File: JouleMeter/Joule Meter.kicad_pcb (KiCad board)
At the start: 4 copper layers, 120 x 134.6 mm, 82 parts, among them J1 XT60-M, J2 XT60-M, J3 22035035, J4 22035035, U1 LMR36510, U3 INA240A1PW, U4 ADS1118IDGS-Q1, U5 MCP6286T-E/OT1

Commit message: Patrick Feedback
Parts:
- removed TP14: VF-V-, TestPoint:TestPoint_Pad_1.0x1.0mm
- moved R12 22.5 mm to (131.3, 64.5), turned to -90 degrees
- moved TP3 19.8 mm to (88.0, 37.0)
- moved C4 15.5 mm to (108.5, 39.0)
- moved TP21 13.3 mm to (128.6, 69.5)
- moved R8 10.5 mm to (116.5, 83.5), turned to 0 degrees
- moved R9 10.4 mm to (131.6, 69.5)
- moved R7 8.94 mm to (122.4, 83.8), turned to 0 degrees
- moved REF** 7.71 mm to (191.7, 163.2)
- moved Nucleo_F44RE2 7.71 mm to (151.6, 124.7)
- moved R13 7.71 mm to (187.9, 115.7)
- moved C20 6.96 mm to (189.9, 131.7)
- moved C22 6.96 mm to (187.9, 131.7)
- moved TP22 5.85 mm to (128.4, 74.0)
- moved TP23 5.85 mm to (128.4, 72.0)
- moved TP4 5.35 mm to (90.0, 71.0)
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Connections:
- U1 pad 16: (no net) -> GND
- U1 pad 9: unconnected-(U1-PAD-Pad9) -> GND
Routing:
- net /Voltage Follower: track 0.00 -> 17.7 mm
- net +3V3D: track 0.00 -> 15.5 mm, vias 0 -> 3
- net +3V3A: track 0.00 -> 13.5 mm, vias 0 -> 4
- net /Current_Sense: track 0.00 -> 13.1 mm
- net GND: track 0.00 -> 12.7 mm, vias 0 -> 12
- net /CS: track 0.00 -> 8.65 mm
- net Net-(U4-AIN1): track 0.00 -> 6.91 mm
- net Net-(J1-POS): track 0.00 -> 6.88 mm
- net Net-(U4-AIN0): track 0.00 -> 6.70 mm
- net Net-(U5-+): track 0.00 -> 6.67 mm
- net Net-(U1-VCC): track 0.00 -> 6.61 mm
- net /FB: track 0.00 -> 6.37 mm
- net Net-(U1-BOOT): track 0.00 -> 6.16 mm
- net /MISO: track 0.00 -> 5.53 mm
- net Net-(J2-POS): track 0.00 -> 5.01 mm
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- added copper zone on F.Cu, net +3V3A
- added copper zone on In1.Cu, net +3V3A
- added copper zone on F.Cu, net +3V3D
- added copper zone on In1.Cu, net +3V3D
- added copper zone on F.Cu, net +5V
- added copper zone on In1.Cu, net +5V
- added copper zone on F.Cu, net +7V
- added copper zone on F.Cu, net Net-(U1-SW)
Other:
- board size 120 x 134.6 mm -> 120 x 143.7 mm

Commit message: Complete Draft Layout
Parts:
- added REF**: SEM_logo, SMV_Logo:SEM_logo, F.Cu at (97.2, 135.5)
- added TP14: VF-V-, TestPoint:TestPoint_Pad_1.0x1.0mm, F.Cu at (122.2, 56.8)
- FERITE_BEAD1: value FB2 -> FB1
- moved TP1 47.7 mm to (111.0, 78.5)
- moved TP3 19.0 mm to (106.8, 39.8)
- moved C4 14.9 mm to (93.8, 40.8)
- moved C2 14.7 mm to (117.2, 40.8)
- moved TP2 14.6 mm to (130.8, 39.0)
- moved REF** 9.21 mm to (78.2, 165.2)
- moved R8 7.50 mm to (122.4, 78.9)
- moved R7 6.79 mm to (122.5, 77.0), turned to 180 degrees
- moved C20 4.18 mm to (191.2, 127.7)
- moved C22 4.18 mm to (189.2, 127.7)
- moved R13 4.18 mm to (189.2, 111.7)
- moved Nucleo_F44RE2 4.06 mm to (152.8, 120.8)
- moved TP16 2.87 mm to (101.2, 80.5)
- moved C21 2.48 mm to (99.1, 84.3)
- moved C23 2.48 mm to (87.1, 79.3)
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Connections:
- net /CAN_H renamed /CAN_P
- net /CAN_L renamed /CAN_N
- C21 pad 1: +3V3D -> +3V3
- MCP2562 pad 5: +3V3D -> +3V3
- R13 pad 1: /Nucleo_F446RE/NUCLEO_1 -> Net-(Nucleo_F44RE2-VBAT)
- U1 pad 10: (no net) -> GND
- U1 pad 11: (no net) -> GND
- U1 pad 12: (no net) -> GND
- U1 pad 13: (no net) -> GND
- U1 pad 14: (no net) -> GND
- U1 pad 15: (no net) -> GND
- U1 pad 17: (no net) -> GND
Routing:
- net /CAN_RXD: track 0.00 -> 76.8 mm, vias 0 -> 1
- net /CAN-TXD: track 0.00 -> 75.4 mm, vias 0 -> 1
- net Net-(Nucleo_F44RE2-PA5): track 1.25 -> 62.2 mm
- net Net-(Nucleo_F44RE2-PA4): track 1.35 -> 62.3 mm
- net Net-(Nucleo_F44RE2-PA6): track 1.20 -> 62.0 mm
- net Net-(Nucleo_F44RE2-PA7): track 1.25 -> 62.0 mm
- net /CAN_N: track 0.00 -> 53.4 mm
- net /CAN_P: track 0.00 -> 48.8 mm
- net Net-(Nucleo_F44RE2-VBAT): track 0.00 -> 23.0 mm
- net /Nucleo_F446RE/NUCLEO_1: track 0.00 -> 14.4 mm
- net Net-(U4-AIN2): track 0.00 -> 7.53 mm
- net GND: track 12.7 -> 7.10 mm, vias 12 -> 344
- net +5V: track 1.71 -> 5.44 mm, vias 8 -> 9
- net Net-(J1-POS): track 6.88 -> 9.75 mm
- net +3V3: track 0.00 -> 2.25 mm
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- added copper zone on F.Cu, net GND
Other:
- board size 120 x 143.7 mm -> 120.5 x 143.7 mm
- board text added: "High Powered Joulemeter (w/Current Sense) 11/16/2025 University of California, Los Angeles By Sergio Gonzalez"
- board text removed: "By Sergio Gonzalez"

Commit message: PCB Complete Draft
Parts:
- removed TP19: CT-RXD, TestPoint:TestPoint_Pad_1.0x1.0mm
- removed TP20: CT-TXD, TestPoint:TestPoint_Pad_1.0x1.0mm
- added J5: M22-7130442, SMV_Joule:HARWIN_M22-7130442, F.Cu at (83.0, 79.1)
- moved R14 48.6 mm to (179.6, 79.5)
- moved TP18 48.3 mm to (176.4, 78.8), turned to 0 degrees
- moved R9 47.6 mm to (115.0, 114.9)
- moved TP21 47.5 mm to (112.2, 114.9), turned to 0 degrees
- moved TP22 45.8 mm to (112.1, 117.5), turned to 0 degrees
- moved R10 45.7 mm to (115.0, 117.5)
- moved TP23 43.2 mm to (112.2, 112.8), turned to 0 degrees
- moved R11 43.0 mm to (115.2, 112.7)
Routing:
- net /MISO: track 5.53 -> 78.1 mm, vias 0 -> 2
- net /SCLK: track 4.87 -> 76.5 mm, vias 0 -> 2
- net /MOSI: track 4.27 -> 74.8 mm, vias 0 -> 2
- net Net-(Nucleo_F44RE2-PA7): track 62.0 -> 7.93 mm, vias 1 -> 0
- net Net-(Nucleo_F44RE2-PA5): track 62.2 -> 8.62 mm, vias 1 -> 0
- net /CS: track 9.99 -> 60.7 mm, vias 0 -> 2
- net Net-(Nucleo_F44RE2-PA6): track 62.0 -> 13.2 mm, vias 1 -> 0
- net Net-(Nucleo_F44RE2-PA4): track 62.3 -> 14.1 mm, vias 1 -> 0
- net /CAN-TXD: track 75.4 -> 79.6 mm, vias 1 -> 0
- net /CAN_RXD: track 76.8 -> 79.6 mm, vias 1 -> 0
- net GND: vias 344 -> 349

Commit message: Revised Version Part 1
Implemented changes from Google Docs and Dylan
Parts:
- C19: value C19 -> 0.1uF
- R0: footprint SMV_Joule:WSBS8518_VIS-L -> SMV_Joule:RESC10052X145N
- U6: renamed from MCP2562; value U6 -> MCP2562
- moved R13 67.8 mm to (211.5, 47.7)
- moved J5 54.3 mm to (137.0, 85.0), turned to -90 degrees
- moved TP22 52.1 mm to (134.8, 70.7)
- moved R10 52.0 mm to (137.8, 70.7)
- moved TP23 50.0 mm to (134.7, 68.1)
- moved R11 49.9 mm to (137.8, 68.1)
- moved Nucleo_F44RE2 48.5 mm to (175.2, 77.8)
- moved REF** 48.2 mm to (213.0, 122.0)
- moved C20 48.1 mm to (213.6, 85.2)
- moved C22 48.1 mm to (211.6, 85.2)
- moved R14 47.8 mm to (195.2, 34.3)
- moved R9 47.2 mm to (137.8, 73.5)
- moved TP21 47.2 mm to (134.9, 73.5)
- moved TP18 46.9 mm to (191.5, 34.3)
- moved REF** 44.6 mm to (67.0, 122.0)
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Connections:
- C21 pad 1: +3V3 -> +3V3A
- U6 pad 5: +3V3 -> +3V3A
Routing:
- net /MISO: track 78.1 -> 17.7 mm, vias 2 -> 0
- net /CAN_RXD: track 79.6 -> 20.8 mm
- net /MOSI: track 74.8 -> 16.7 mm, vias 2 -> 0
- net /CAN-TXD: track 79.6 -> 24.4 mm
- net /SCLK: track 76.5 -> 24.7 mm
- net /CS: track 60.7 -> 95.8 mm, vias 2 -> 0
- net /Nucleo_F446RE/NUCLEO_1: track 14.4 -> 35.4 mm
- net Net-(Nucleo_F44RE2-VBAT): track 23.0 -> 4.55 mm
- net +7V: track 1.00 -> 11.8 mm
- net +3V3D: track 15.5 -> 4.91 mm
- net /Voltage Follower: track 17.7 -> 7.55 mm
- net /CAN_N: track 53.4 -> 46.1 mm
- net Net-(J1-POS): track 9.75 -> 2.58 mm, vias 0 -> 29
- net Net-(Nucleo_F44RE2-PA4): track 14.1 -> 20.0 mm
- net +5V: track 5.44 -> 11.3 mm
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- added copper zone on In2.Cu, net +3V3A
- added copper zone on In2.Cu, net +3V3D
- added copper zone on In2.Cu, net +5V
- added copper zone on In1.Cu, net GND
- added copper zone on B.Cu, net Net-(J1-POS)
- added copper zone on In2.Cu, net Net-(J1-POS)
- added copper zone on B.Cu, net Net-(J2-POS)
- added copper zone on In2.Cu, net Net-(J2-POS)
- removed copper zone on In1.Cu, net +3V3A
- removed copper zone on In1.Cu, net +3V3D
- removed copper zone on In1.Cu, net +5V
- removed copper zone on In2.Cu, net GND
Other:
- board size 120.5 x 143.7 mm -> 153.8 x 95 mm
- board text added: "High Power Joulemeter (w/Current Sense) 11/24/2025 University of California, Los Angeles By Sergio Gonzalez"
- board text removed: "High Powered Joulemeter (w/Current Sense) 11/16/2025 University of California, Los Angeles By Sergio Gonzalez"

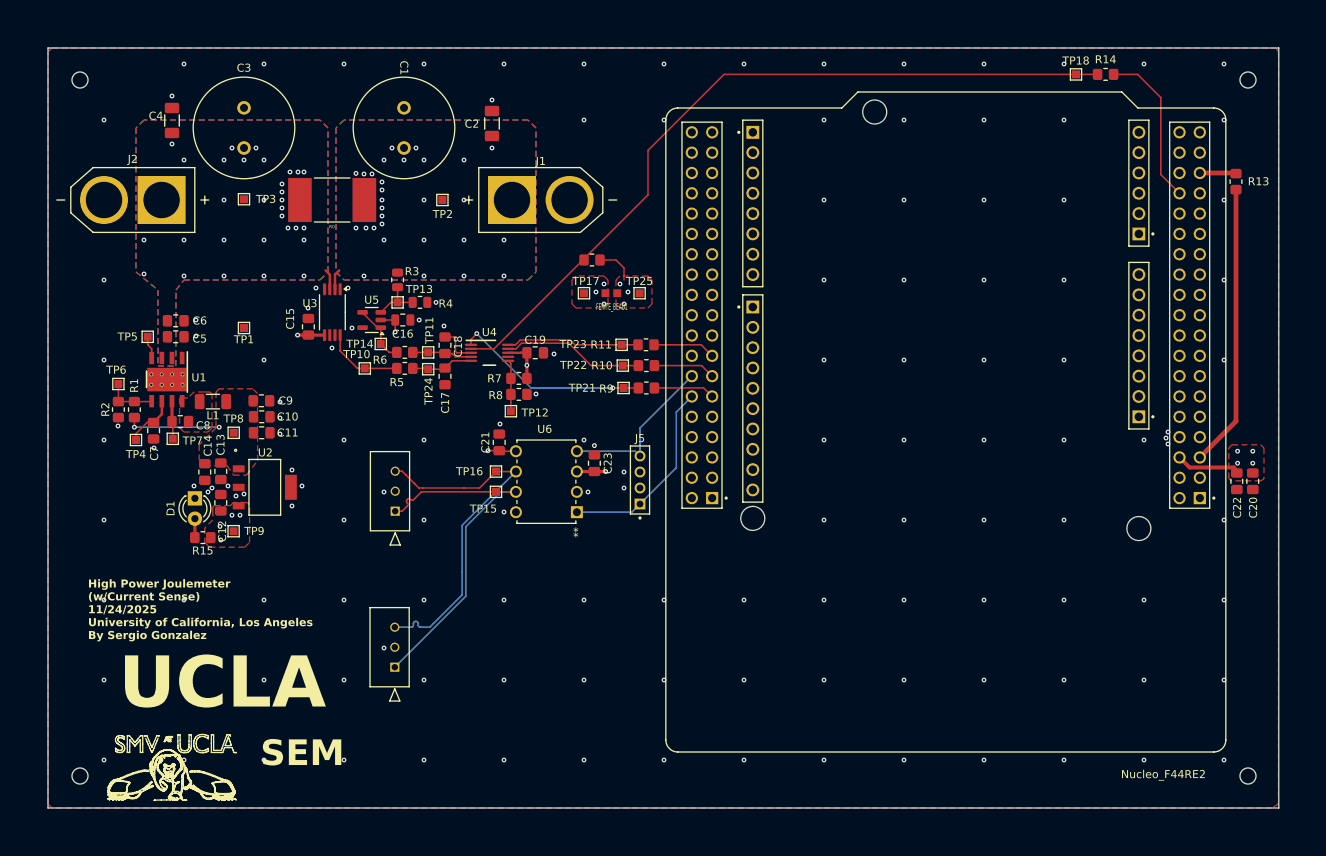
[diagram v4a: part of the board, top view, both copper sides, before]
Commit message: Verification Changes (No Peninsula Fixes)
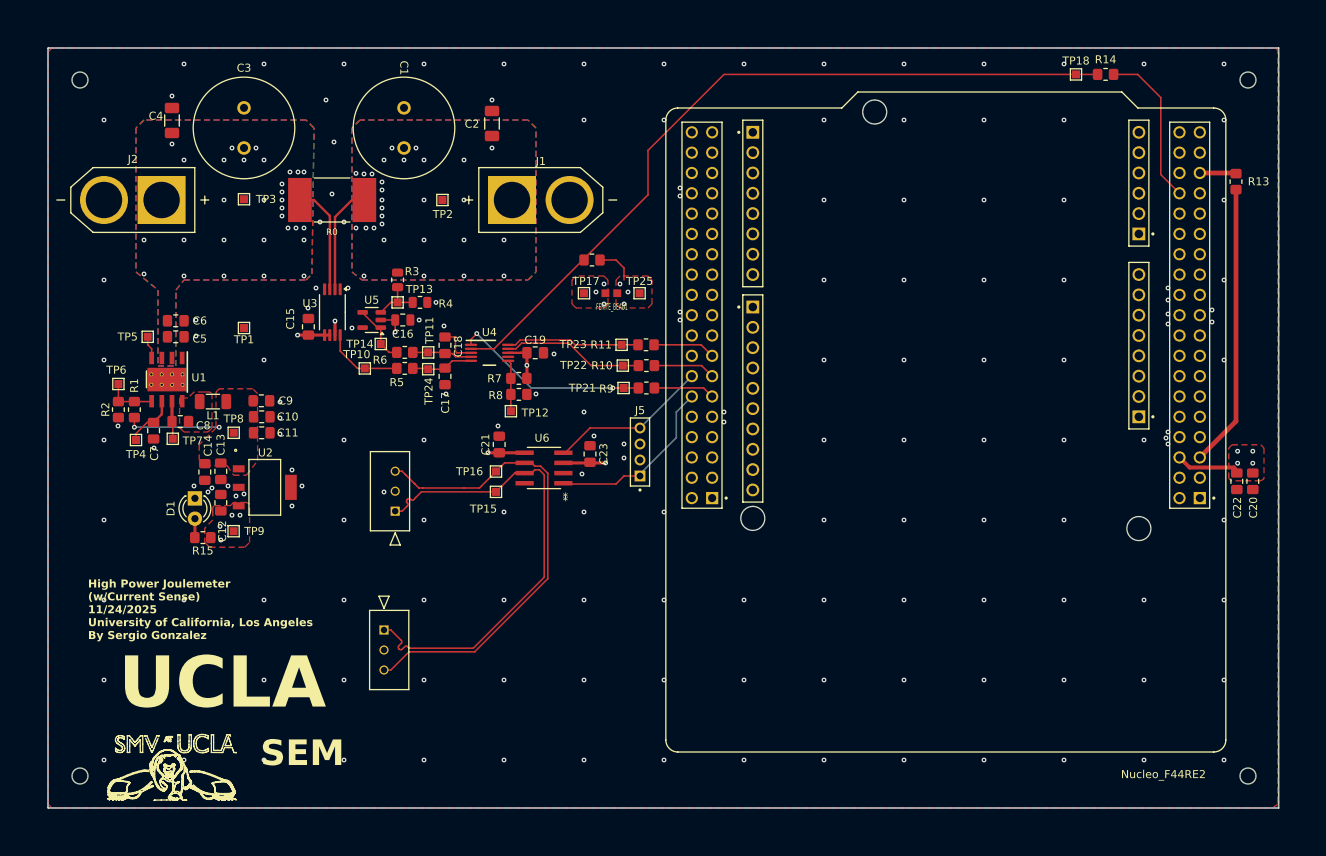
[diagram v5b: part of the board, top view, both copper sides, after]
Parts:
- U6: footprint SMV_Joule:PDIP8_300MC_MCH -> SMV_Joule:SOIC8-N_MC_MCH-M
- moved U6 6.88 mm to (125.0, 83.5)
- moved J4 4.84 mm to (105.0, 103.8), turned to 90 degrees
- moved J5 3.50 mm to (137.0, 81.5)
- moved C23 1.28 mm to (130.8, 81.8)
- moved C21 0.26 mm to (119.4, 80.6)
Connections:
- U3 pad 6: GND -> +3V3A
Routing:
- net /CAN_P: track 46.1 -> 60.6 mm
- net /CAN_N: track 46.1 -> 60.2 mm
- net Net-(J2-POS): track 2.58 -> 13.7 mm
- net Net-(J1-POS): track 2.58 -> 13.6 mm
- net /CAN-TXD: track 24.4 -> 22.7 mm
- net GND: track 5.03 -> 6.80 mm, vias 141 -> 160
- net /CAN_RXD: track 20.8 -> 20.0 mm
- net +3V3A: track 15.5 -> 16.2 mm
- added copper zone on B.Cu, net GND

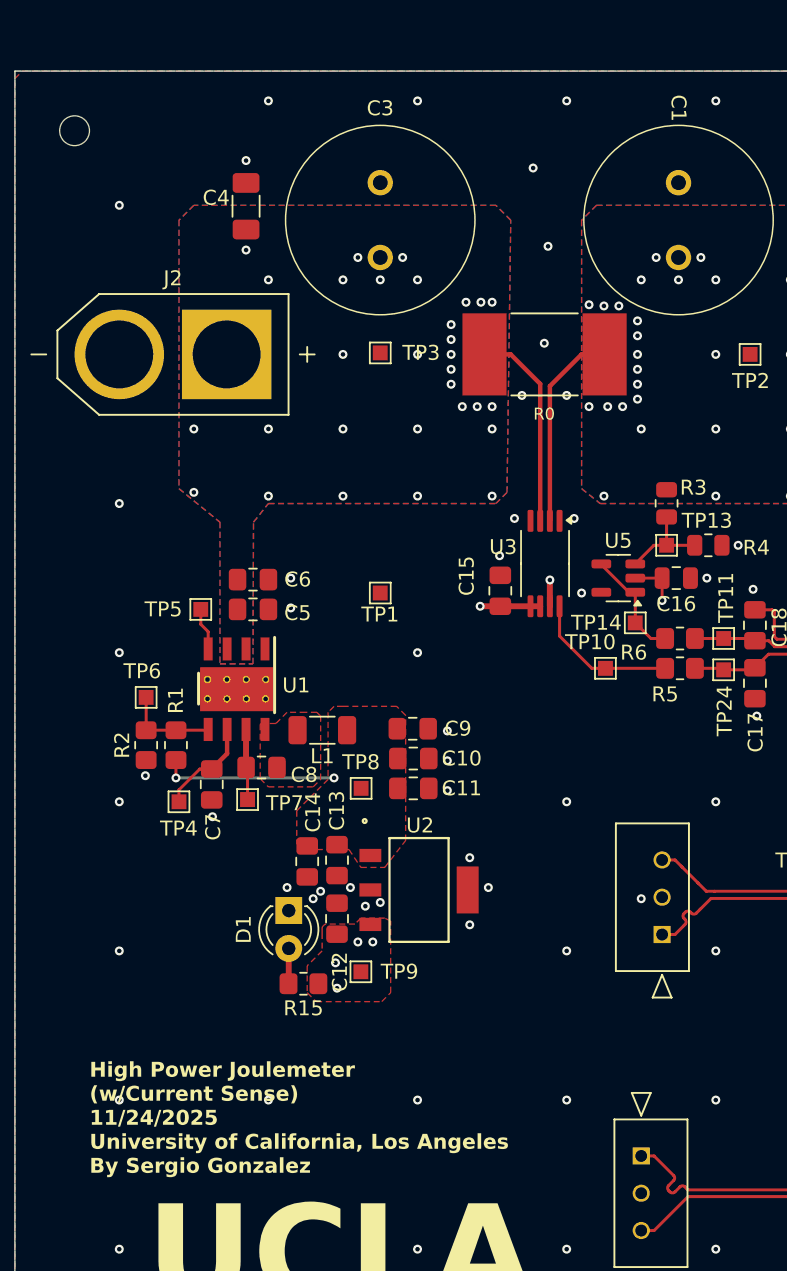
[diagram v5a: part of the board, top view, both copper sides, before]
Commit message: Joule Meter Final
-Removed Pinnulas
-Added specific capacitor links for capacitors with a 48V across.
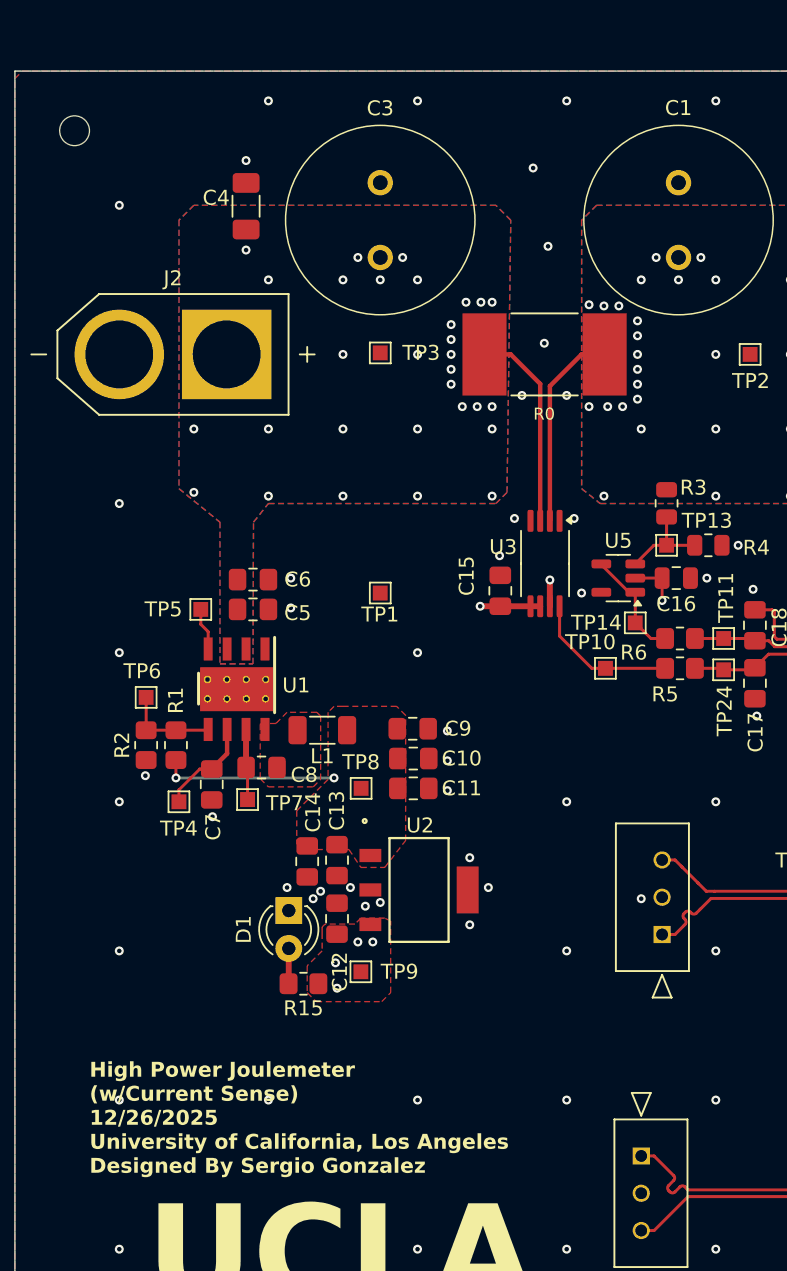
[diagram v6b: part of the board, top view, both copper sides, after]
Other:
- board text added: "High Power Joulemeter (w/Current Sense) 12/26/2025 University of California, Los Angeles Designed By Sergio Gonzalez"
- board text removed: "High Power Joulemeter (w/Current Sense) 11/24/2025 University of California, Los Angeles By Sergio Gonzalez"
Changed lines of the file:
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@@
 		(at 107.5 40.99175 90)
 		(property "Reference" "C1"
-			(at 7.50825 0 270)
+			(at 7.50825 0 0)
 			(unlocked yes)
 			(layer "F.SilkS")
@@
 		(layer "Edge.Cuts")
 	)
-	(gr_text "High Power Joulemeter\n(w/Current Sense)\n11/24/2025\nUniversity of California, Los Angeles\nBy Sergio Gonzalez"
+	(gr_text "High Power Joulemeter\n(w/Current Sense)\n12/26/2025\nUniversity of California, Los Angeles\nDesigned By Sergio Gonzalez"
 		(at 68 105 0)
 		(layer "F.SilkS")
@@
 	)
 	(zone
+		(net 0)
+		(net_name "")
+		(layer "F.Cu")
+		(hatch edge 0.5)
+		(connect_pads
+			(clearance 0)
+		)
+		(min_thickness 0.25)
+		(filled_areas_thickness no)
+		(keepout
+			(tracks allowed)
+			(vias allowed)
+			(pads allowed)
+			(copperpour not_allowed)
+			(footprints allowed)
+		)
+		(placement
+			(enabled no)
+			(sheetname "")
+		)
+		(fill
+			(thermal_gap 0.5)
+			(thermal_bridge_width 0.5)
+		)
+		(polygon
+			(pts
+				(xy 96.2 60.4) (xy 97.8 60.4) (xy 97.8 51.8) (xy 96.6 51.2)
+			)
+		)
+	)
+	(zone
 		(net 1)
 		(net_name "GND")
@@
 	)
 	(zone
+		(net 0)
+		(net_name "")
+		(layer "F.Cu")
+		(hatch edge 0.5)
+		(connect_pads
+			(clearance 0)
+		)
+		(min_thickness 0.25)
+		(filled_areas_thickness no)
+		(keepout
+			(tracks allowed)
+			(vias allowed)
+			(pads allowed)
+			(copperpour not_allowed)
+			(footprints allowed)
+		)
+		(placement
+			(enabled no)
+			(sheetname "")
+		)
+		(fill
+			(thermal_gap 0.5)
+			(thermal_bridge_width 0.5)
+		)
+		(polygon
+			(pts
+				(xy 99.4 60.4) (xy 100.8 60.4) (xy 100.8 51.8) (xy 100.4 51.4) (xy 99.4 51.4)
+			)
+		)
+	)
+	(zone
 		(net 9)
 		(net_name "+5V")
@@
 	)
 	(zone
+		(net 0)
+		(net_name "")
+		(layer "F.Cu")
+		(hatch edge 0.5)
+		(connect_pads
+			(clearance 0)
+		)
+		(min_thickness 0.25)
+		(filled_areas_thickness no)
+		(keepout
+			(tracks allowed)
+			(vias allowed)
+			(pads allowed)
+			(copperpour not_allowed)
+			(footprints allowed)
+		)
+		(placement
+			(enabled no)
+			(sheetname "")
+		)
+		(fill
+			(thermal_gap 0.5)
+			(thermal_bridge_width 0.5)
+		)
+		(polygon
+			(pts
+				(xy 202.5 46.8) (xy 202.8 47.1) (xy 203.4 47.1) (xy 203.9 46.6) (xy 203.9 40.5) (xy 203.4 40) (xy 202.5 40)
+			)
+		)
+	)
+	(zone
 		(net 7)
 		(net_name "Net-(U1-SW)")
@@
 	)
 	(zone
+		(net 0)
+		(net_name "")
+		(layer "F.Cu")
+		(hatch edge 0.5)
+		(connect_pads
+			(clearance 0)
+		)
+		(min_thickness 0.25)
+		(filled_areas_thickness no)
+		(keepout
+			(tracks allowed)
+			(vias allowed)
+			(pads allowed)
+			(copperpour not_allowed)
+			(footprints allowed)
+		)
+		(placement
+			(enabled no)
+			(sheetname "")
+		)
+		(fill
+			(thermal_gap 0.5)
+			(thermal_bridge_width 0.5)
+		)
+		(polygon
+			(pts
+				(xy 142.6 73.2) (xy 142.6 70.6) (xy 134.2 70.6) (xy 133.6 71.2) (xy 133.6 73) (xy 133.8 73.2)
+			)
+		)
+	)
+	(zone
 		(net 8)
 		(net_name "+7V")
@@
 			)
 		)
+	)
+	(zone
+		(net 0)
+		(net_name "")
+		(layer "In2.Cu")
+		(hatch edge 0.5)
+		(connect_pads
+			(clearance 0)
+		)
+		(min_thickness 0.25)
+		(filled_areas_thickness no)
+		(keepout
+			(tracks allowed)
+			(vias allowed)
+			(pads allowed)
+			(copperpour not_allowed)
+			(footprints allowed)
+		)
+		(placement
+			(enabled no)
+			(sheetname "")
+		)
+		(fill
+			(thermal_gap 0.5)
+			(thermal_bridge_width 0.5)
+		)
+		(polygon
+			(pts
+				(xy 146.1 61.7) (xy 146.1 80.1) (xy 150.6 80.1) (xy 150.6 62.5) (xy 150.2 62.1) (xy 146.5 62.1)
+			)
+		)
